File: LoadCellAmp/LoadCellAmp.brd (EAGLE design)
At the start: 37.8 x 10.2 mm, 19 parts, among them IC1 AD623RM

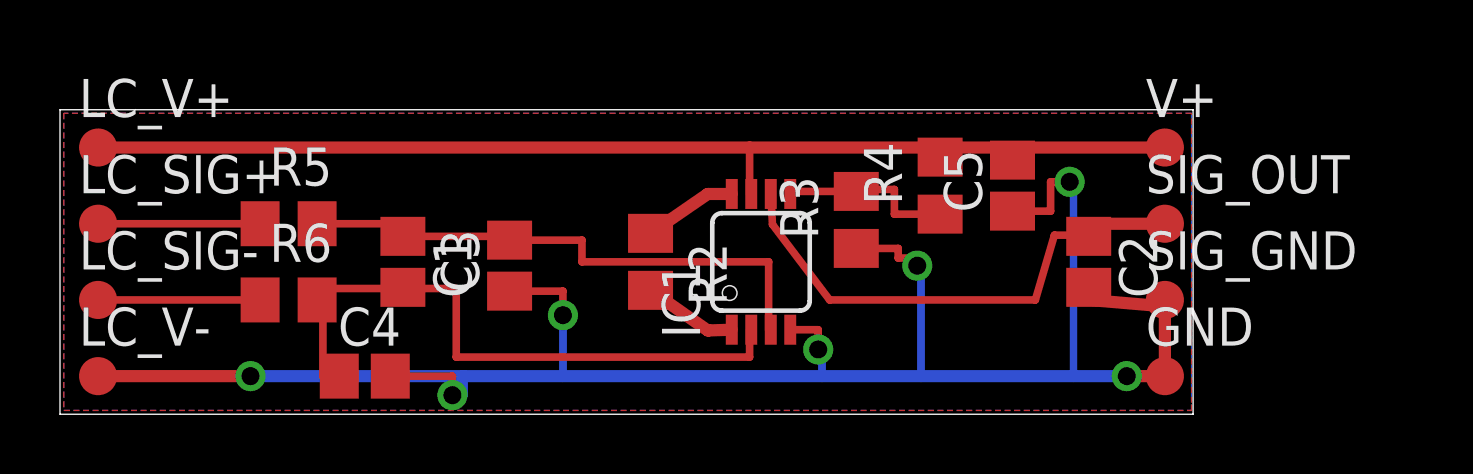
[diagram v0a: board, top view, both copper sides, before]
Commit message: BOM for the LoadCellAmp
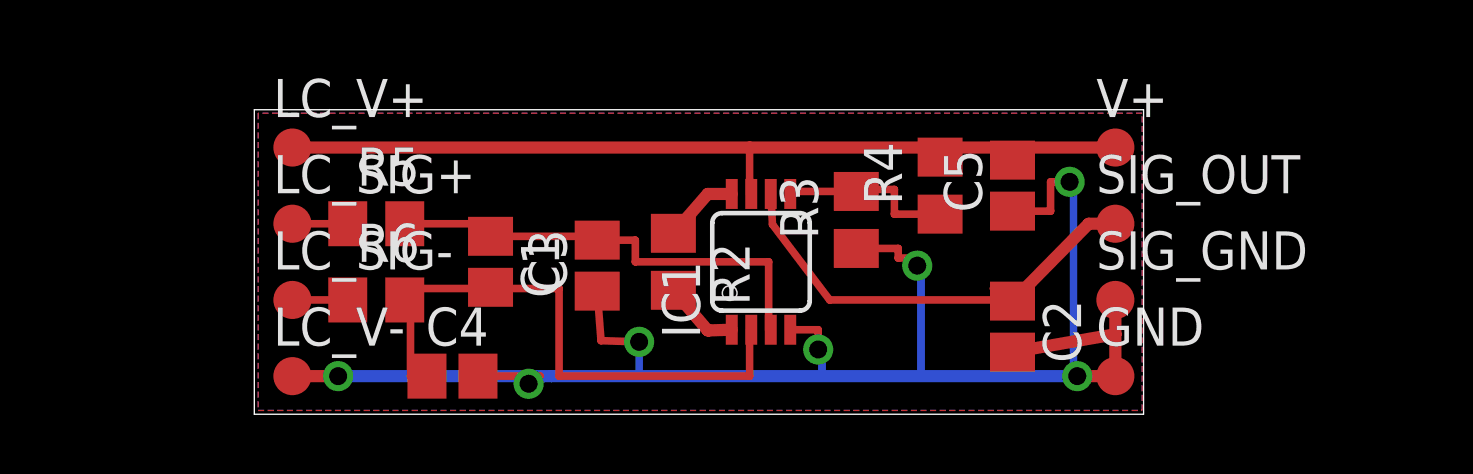
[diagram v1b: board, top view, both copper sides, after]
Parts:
- moved LC_SIG+ 6.48 mm to (7.75, 6.35)
- moved LC_SIG- 6.48 mm to (7.75, 3.81)
- moved LC_V+ 6.48 mm to (7.75, 8.89)
- moved LC_V- 6.48 mm to (7.75, 1.27)
- moved C2 3.33 mm to (31.8, 2.92)
- moved C1 2.92 mm to (14.4, 5.08)
- moved R5 2.92 mm to (10.5, 6.35)
- moved R6 2.92 mm to (10.5, 3.81)
- moved C3 2.92 mm to (17.9, 4.95)
- moved C4 2.92 mm to (13.1, 1.27)
- moved GND 1.65 mm to (35.2, 1.27)
- moved SIG_GND 1.65 mm to (35.2, 3.81)
- moved SIG_OUT 1.65 mm to (35.2, 6.35)
- moved V+ 1.65 mm to (35.2, 8.89)
- moved R2 0.76 mm to (20.4, 5.08)
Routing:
- net GND: track 67.9 -> 59.4 mm
- net +5V: track 37.9 -> 29.8 mm
- net N$7: track 5.40 -> 1.84 mm
- net N$6: track 5.40 -> 1.84 mm
- net N$8: track 18.7 -> 15.7 mm
- net N$9: track 21.4 -> 19.7 mm
- net N$2: track 3.12 -> 2.54 mm
- net N$1: track 3.13 -> 2.56 mm
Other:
- board size 37.8 x 10.2 mm -> 29.6 x 10.2 mm

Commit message: Added marker, rearranged silkscreen
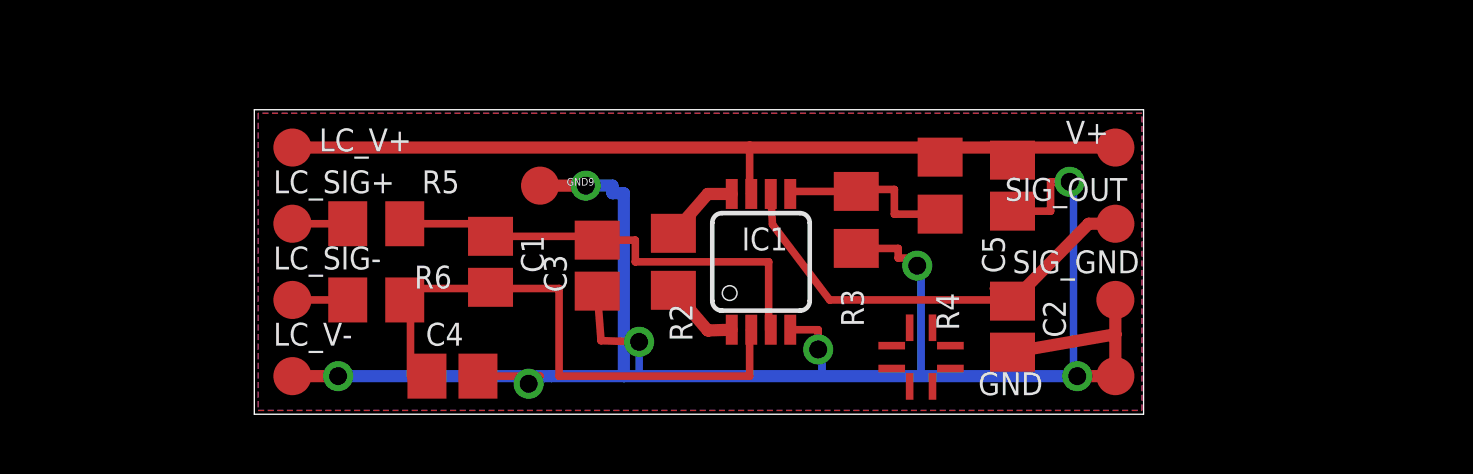
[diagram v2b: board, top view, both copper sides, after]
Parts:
- added GND9: TPB1,27, testpad:B1,27
- added U$2: (no value), marks:PASSER
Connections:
- net GND: now also GND9.TP
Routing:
- net GND: track 59.4 -> 68.5 mm, vias 7 -> 8

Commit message: Chenged values of R and C.
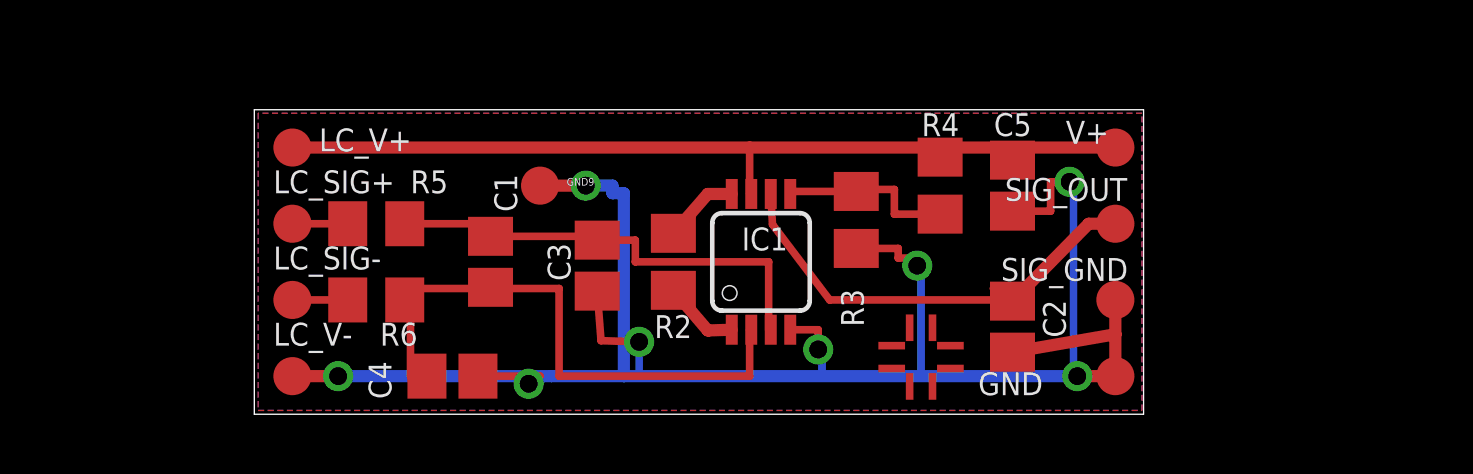
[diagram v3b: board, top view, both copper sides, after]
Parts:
- C1, C2, C3, C4, C5: value (none) -> 1uF
- R5, R6: value (none) -> 16k
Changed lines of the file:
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@@
 <attribute name="VALUE" x="27.051" y="5.08" size="0.762" layer="27" ratio="10" rot="R180"/>
 </element>
-<element name="C1" library="resistor" package="C0805" value="" x="14.351" y="5.08" smashed="yes" rot="R270">
-<attribute name="NAME" x="15.367" y="5.969" size="0.762" layer="25" rot="R270"/>
-<attribute name="VALUE" x="12.065" y="5.969" size="1.27" layer="27" rot="R270"/>
+<element name="C1" library="resistor" package="C0805" value="1uF" x="14.351" y="5.08" smashed="yes" rot="R270">
+<attribute name="NAME" x="14.478" y="8.001" size="0.762" layer="25" rot="R270"/>
+<attribute name="VALUE" x="13.589" y="8.382" size="0.762" layer="27" rot="R270"/>
 </element>
 <element name="R2" library="rcl" package="R0805" value="100" x="20.447" y="5.08" smashed="yes" rot="R270">
-<attribute name="NAME" x="20.32" y="3.683" size="0.762" layer="25" rot="R270"/>
-<attribute name="VALUE" x="19.812" y="8.509" size="0.762" layer="27" rot="R270"/>
+<attribute name="NAME" x="19.812" y="2.54" size="0.762" layer="25"/>
+<attribute name="VALUE" x="19.685" y="6.985" size="0.762" layer="27"/>
 </element>
 <element name="LC_V+" library="testpad" package="B1,27" value="TPB1,27" x="7.747" y="8.89" smashed="yes">
@@
 <element name="SIG_GND" library="testpad" package="B1,27" value="TPB1,27" x="35.179" y="3.81" smashed="yes">
 <attribute name="TP_SIGNAL_NAME" value="" x="34.544" y="1.905" size="1" layer="37"/>
-<attribute name="NAME" x="31.75" y="4.699" size="0.762" layer="25" ratio="10"/>
+<attribute name="NAME" x="31.369" y="4.445" size="0.762" layer="25" ratio="10"/>
 <attribute name="VALUE" x="34.544" y="3.048" size="0.0254" layer="27"/>
 </element>
@@
 </element>
 <element name="R4" library="rcl" package="R0805" value="2k" x="29.337" y="7.62" smashed="yes" rot="R90">
-<attribute name="NAME" x="29.972" y="2.794" size="0.762" layer="25" rot="R90"/>
-<attribute name="VALUE" x="29.972" y="4.826" size="0.762" layer="27" rot="R90"/>
+<attribute name="NAME" x="29.972" y="10.033" size="0.762" layer="25" rot="R180"/>
+<attribute name="VALUE" x="29.972" y="5.715" size="0.762" layer="27" rot="R180"/>
 </element>
-<element name="C2" library="resistor" package="C0805" value="" x="31.75" y="2.921" smashed="yes" rot="R270">
+<element name="C2" library="resistor" package="C0805" value="1uF" x="31.75" y="2.921" smashed="yes" rot="R270">
 <attribute name="NAME" x="32.766" y="3.81" size="0.762" layer="25" rot="R270"/>
-<attribute name="VALUE" x="29.464" y="3.81" size="1.27" layer="27" rot="R270"/>
+<attribute name="VALUE" x="29.972" y="3.81" size="0.762" layer="27" rot="R270"/>
 </element>
-<element name="R5" library="rcl" package="R0805" value="" x="10.541" y="6.35" smashed="yes">
-<attribute name="NAME" x="12.065" y="7.366" size="0.762" layer="25"/>
-<attribute name="VALUE" x="9.906" y="3.81" size="1.27" layer="27"/>
+<element name="R5" library="rcl" package="R0805" value="16k" x="10.541" y="6.35" smashed="yes">
+<attribute name="NAME" x="11.684" y="7.366" size="0.762" layer="25"/>
+<attribute name="VALUE" x="13.081" y="5.461" size="0.762" layer="27" rot="R90"/>
 </element>
-<element name="R6" library="rcl" package="R0805" value="" x="10.541" y="3.81" smashed="yes">
-<attribute name="NAME" x="11.811" y="4.191" size="0.762" layer="25"/>
-<attribute name="VALUE" x="9.906" y="1.27" size="1.27" layer="27"/>
+<element name="R6" library="rcl" package="R0805" value="16k" x="10.541" y="3.81" smashed="yes">
+<attribute name="NAME" x="10.668" y="2.286" size="0.762" layer="25"/>
+<attribute name="VALUE" x="13.081" y="3.048" size="0.762" layer="27" rot="R90"/>
 </element>
-<element name="C3" library="resistor" package="C0805" value="" x="17.907" y="4.953" smashed="yes" rot="R90">
-<attribute name="NAME" x="16.891" y="4.064" size="0.762" layer="25" rot="R90"/>
-<attribute name="VALUE" x="20.193" y="4.064" size="1.27" layer="27" rot="R90"/>
+<element name="C3" library="resistor" package="C0805" value="1uF" x="17.907" y="4.953" smashed="yes" rot="R90">
+<attribute name="NAME" x="17.018" y="4.445" size="0.762" layer="25" rot="R90"/>
+<attribute name="VALUE" x="17.78" y="1.524" size="0.762" layer="27" rot="R90"/>
 </element>
-<element name="C4" library="resistor" package="C0805" value="" x="13.081" y="1.27" smashed="yes">
-<attribute name="NAME" x="12.192" y="2.286" size="0.762" layer="25"/>
-<attribute name="VALUE" x="12.192" y="-1.016" size="1.27" layer="27"/>
+<element name="C4" library="resistor" package="C0805" value="1uF" x="13.081" y="1.27" smashed="yes">
+<attribute name="NAME" x="11.049" y="0.508" size="0.762" layer="25" rot="R90"/>
+<attribute name="VALUE" x="12.827" y="2.032" size="0.762" layer="27"/>
 </element>
-<element name="C5" library="resistor" package="C0805" value="" x="31.75" y="7.62" smashed="yes" rot="R90">
-<attribute name="NAME" x="31.496" y="4.699" size="0.762" layer="25" rot="R90"/>
-<attribute name="VALUE" x="34.036" y="6.731" size="1.27" layer="27" rot="R90"/>
+<element name="C5" library="resistor" package="C0805" value="1uF" x="31.75" y="7.62" smashed="yes" rot="R90">
+<attribute name="NAME" x="32.385" y="10.033" size="0.762" layer="25" rot="R180"/>
+<attribute name="VALUE" x="32.512" y="5.969" size="0.762" layer="27" rot="R180"/>
 </element>
 <element name="GND9" library="testpad" package="B1,27" value="TPB1,27" x="16.002" y="7.62" smashed="yes">
